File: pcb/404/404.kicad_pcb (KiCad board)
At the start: 2 copper layers, 52 x 63 mm, 43 parts, among them J1 Conn_01x04, Q1 BC846, U1 RC4558

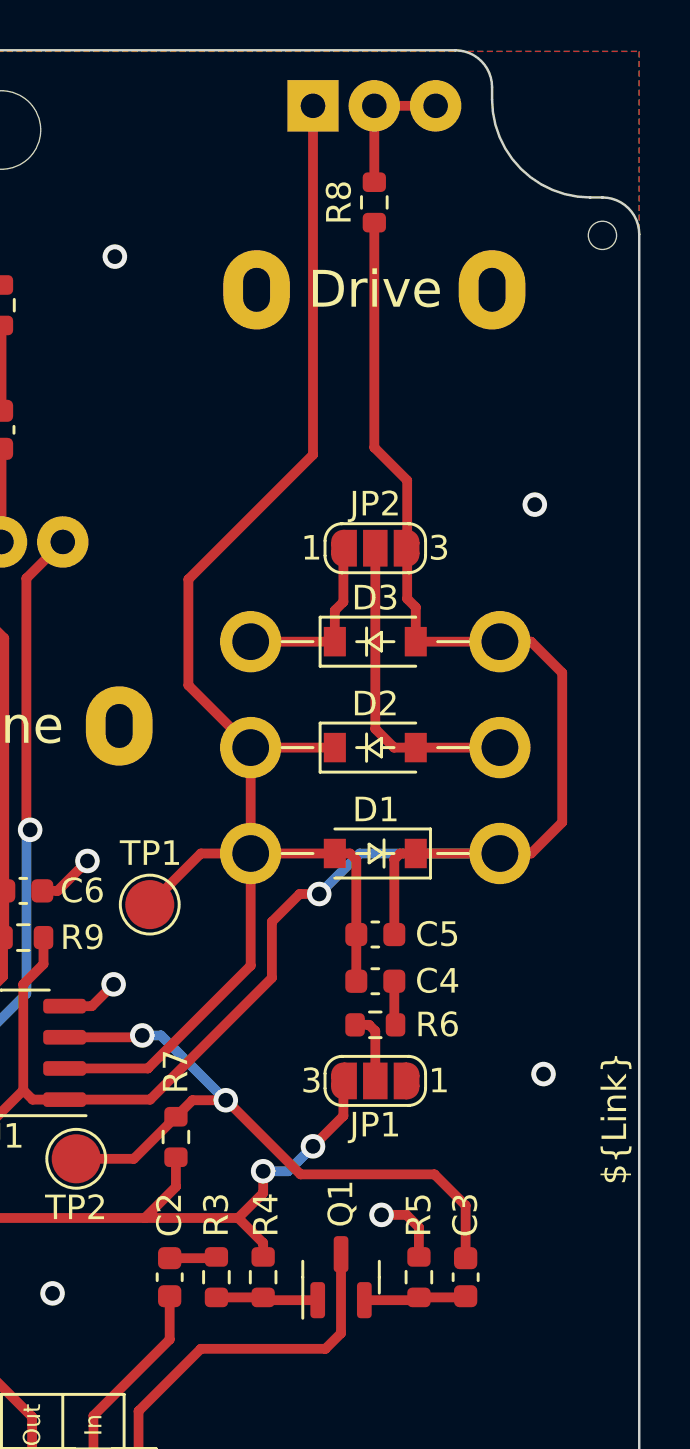
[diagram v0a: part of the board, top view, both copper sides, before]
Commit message: [404] Rename board; Update silk jumper description
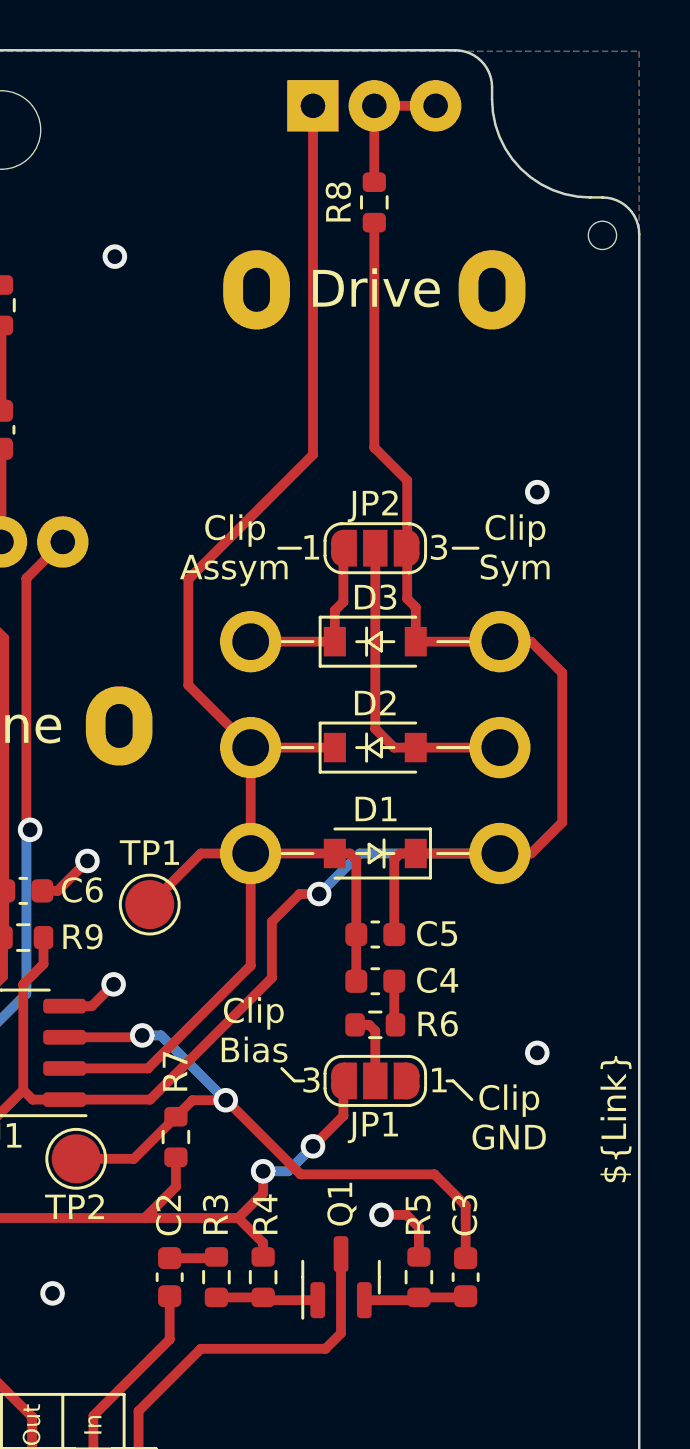
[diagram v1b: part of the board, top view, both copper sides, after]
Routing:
- net Net-(C4-Pad1): track 66.1 -> 65.3 mm
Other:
- board text added: "Clip Assym"
- board text added: "Clip Bias"
- board text added: "Clip GND"
- board text added: "Clip Sym"
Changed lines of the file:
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@@
   (gr_line (start 152 122.295) (end 152 124.561) (layer "F.SilkS") (width 0.12))
   (gr_line (start 144.5 122.295) (end 144.5 124.561) (layer "F.SilkS") (width 0.12))
+  (gr_line (start 167.915 87.799) (end 168.931 87.799) (layer "F.SilkS") (width 0.12))
+  (gr_line (start 161.692 87.799) (end 160.803 87.799) (layer "F.SilkS") (width 0.12))
   (gr_line (start 149.5 122.295) (end 149.5 124.561) (layer "F.SilkS") (width 0.12))
+  (gr_line (start 167.915 109.516) (end 168.677 110.278) (layer "F.SilkS") (width 0.12))
   (gr_line (start 144.5 122.295) (end 154.5 122.295) (layer "F.SilkS") (width 0.12))
   (gr_line (start 147 122.295) (end 147 124.545) (layer "F.SilkS") (width 0.12))
+  (gr_line (start 161.819 109.516) (end 161.438 109.516) (layer "F.SilkS") (width 0.12))
   (gr_line (start 154.5 122.295) (end 154.5 124.561) (layer "F.SilkS") (width 0.12))
+  (gr_line (start 161.438 109.516) (end 160.93 109.008) (layer "F.SilkS") (width 0.12))
+  (gr_line (start 167.661 109.516) (end 167.915 109.516) (layer "F.SilkS") (width 0.12))
   (gr_line (start 149.5 67.545) (end 149.5 130.545) (layer "Eco1.User") (width 0.15))
   (gr_line (start 125 73.5) (end 125.5 73.5) (layer "Edge.Cuts") (width 0.1))
@@
     (effects (font (size 1.5 1.5) (thickness 0.3)))
   )
+  (gr_text "Clip\nGND" (at 170.201 111.04) (layer "F.SilkS")
+    (effects (font (size 1 1) (thickness 0.15)))
+  )
+  (gr_text "Clip\nBias" (at 159.787 107.484) (layer "F.SilkS")
+    (effects (font (size 1 1) (thickness 0.15)))
+  )
   (gr_text "${Commit}" (at 163 127.545) (layer "F.SilkS")
     (effects (font (size 1 1) (thickness 0.2)))
@@
   (gr_text "Out" (at 150.75 123.545 90) (layer "F.SilkS")
     (effects (font (size 0.7 0.7) (thickness 0.13)))
+  )
+  (gr_text "Clip\nSym" (at 170.455 87.799) (layer "F.SilkS")
+    (effects (font (size 1 1) (thickness 0.15)))
   )
   (gr_text "Vol" (at 134.26 77.258) (layer "F.SilkS")
     (effects (font (size 1.5 1.5) (thickness 0.3)))
+  )
+  (gr_text "Clip\nAssym" (at 159.025 87.799) (layer "F.SilkS")
+    (effects (font (size 1 1) (thickness 0.15)))
   )
   (gr_text "Drive" (at 164.74 77.258) (layer "F.SilkS")
@@
   (via (at 153.0052 100.5498) (size 1) (drill 0.6) (layers "F.Cu" "B.Cu") (net 2))
   (via (at 154.1228 75.9118) (size 1) (drill 0.6) (layers "F.Cu" "B.Cu") (free) (net 2))
-  (via (at 171.598 109.2366) (size 1) (drill 0.6) (layers "F.Cu" "B.Cu") (free) (net 2))
+  (via (at 171.344 108.373) (size 1) (drill 0.6) (layers "F.Cu" "B.Cu") (free) (net 2))
   (via (at 127.656 101.8706) (size 1) (drill 0.6) (layers "F.Cu" "B.Cu") (free) (net 2))
   (via (at 154.072 105.579) (size 1) (drill 0.6) (layers "F.Cu" "B.Cu") (net 2))
   (via (at 151.5828 118.1774) (size 1) (drill 0.6) (layers "F.Cu" "B.Cu") (free) (net 2))
   (via (at 145 75.9118) (size 1) (drill 0.6) (layers "F.Cu" "B.Cu") (free) (net 2))
-  (via (at 171.2424 86.021) (size 1) (drill 0.6) (layers "F.Cu" "B.Cu") (free) (net 2))
+  (via (at 171.344 85.513) (size 1) (drill 0.6) (layers "F.Cu" "B.Cu") (free) (net 2))
   (via (at 164.994 114.977) (size 1) (drill 0.6) (layers "F.Cu" "B.Cu") (net 2))
   (segment (start 153.25 123.165) (end 153.25 126.975) (width 0.4) (layer "F.Cu") (net 3))
@@
   (segment (start 166.4055 118.4545) (end 166.518 118.342) (width 0.4) (layer "F.Cu") (net 6))
   (segment (start 166.518 118.342) (end 168.373 118.342) (width 0.4) (layer "F.Cu") (net 6))
-  (segment (start 166.568 118.292) (end 166.518 118.342) (width 0.4) (layer "F.Cu") (net 6))
   (segment (start 164.293 118.4545) (end 166.4055 118.4545) (width 0.4) (layer "F.Cu") (net 6))
   (segment (start 168.423 114.596) (end 168.423 116.742) (width 0.4) (layer "F.Cu") (net 7))
@@
   (segment (start 158.644 110.3034) (end 156.0024 107.6618) (width 0.4) (layer "B.Cu") (net 7))
   (segment (start 165.515 107.18) (end 165.565 107.23) (width 0.4) (layer "F.Cu") (net 8))
-  (segment (start 165.565 105.502) (end 165.515 105.452) (width 0.4) (layer "F.Cu") (net 8))
   (segment (start 165.515 105.452) (end 165.515 107.18) (width 0.4) (layer "F.Cu") (net 8))
   (segment (start 159.66 95.927) (end 163.09 95.927) (width 0.4) (layer "F.Cu") (net 9))
@@
   (segment (start 157.12 89.069) (end 157.12 93.387) (width 0.4) (layer "F.Cu") (net 9))
   (segment (start 155.5452 102.3278) (end 157.628 100.245) (width 0.4) (layer "F.Cu") (net 9))
-  (segment (start 158.898 95.927) (end 159.66 95.927) (width 0.4) (layer "F.Cu") (net 9))
   (segment (start 162.2 83.989) (end 157.12 89.069) (width 0.4) (layer "F.Cu") (net 9))
   (segment (start 157.12 93.387) (end 159.66 95.927) (width 0.4) (layer "F.Cu") (net 9))
@@
   (segment (start 164.7 72.877) (end 164.7 69.765) (width 0.4) (layer "F.Cu") (net 20))
   (segment (start 164.7 69.765) (end 167.2 69.765) (width 0.4) (layer "F.Cu") (net 20))
-  (segment (start 164.7 69.765) (end 164.651663 69.765) (width 0.4) (layer "F.Cu") (net 20))
   (segment (start 146.925 107.738) (end 143.467 107.738) (width 0.4) (layer "F.Cu") (net 21))
   (segment (start 148.865 107.611) (end 148.738 107.738) (width 0.4) (layer "F.Cu") (net 21))

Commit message: [404] Export gerbers/pos/bom
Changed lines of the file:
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@@
       (layerselection 0x00010fc_ffffffff)
       (disableapertmacros false)
-      (usegerberextensions false)
-      (usegerberattributes true)
-      (usegerberadvancedattributes true)
-      (creategerberjobfile true)
+      (usegerberextensions true)
+      (usegerberattributes false)
+      (usegerberadvancedattributes false)
+      (creategerberjobfile false)
       (svguseinch false)
       (svgprecision 6)
       (excludeedgelayer true)
       (plotframeref false)
-      (viasonmask false)
+      (viasonmask true)
       (mode 1)
       (useauxorigin false)
@@
       (plotinvisibletext false)
       (sketchpadsonfab false)
-      (subtractmaskfromsilk false)
+      (subtractmaskfromsilk true)
       (outputformat 1)
       (mirror false)
-      (drillshape 1)
+      (drillshape 0)
       (scaleselection 1)
-      (outputdirectory "")
-    )
-  )
-  (property "Commit" "Commit")
+      (outputdirectory "../../_gitignored/Gerbers/404/Pos/")
+    )
+  )
+  (property "Commit" "87d2bbb")
   (property "Link" "gitlab.com/Chrismettal/pedaldev")
   (property "Name" "404")
@@
     (fp_line (start -1.6 0.8) (end -1.6 -0.8) (layer "F.Fab") (width 0.1))
     (fp_line (start 1.6 0.8) (end -1.6 0.8) (layer "F.Fab") (width 0.1))
-    (pad "1" smd roundrect (at -1.475 0 270) (size 1.15 1.8) (layers "F.Cu" "F.Paste" "F.Mask") (roundrect_rratio 0.217391)
+    (pad "1" smd roundrect (at -1.475 0 270) (size 1.15 1.8) (layers "F.Cu" "F.Paste" "F.Mask") (roundrect_rratio 0.2173913043)
       (net 22 "+4V5") (pintype "passive"))
-    (pad "2" smd roundrect (at 1.475 0 270) (size 1.15 1.8) (layers "F.Cu" "F.Paste" "F.Mask") (roundrect_rratio 0.217391)
+    (pad "2" smd roundrect (at 1.475 0 270) (size 1.15 1.8) (layers "F.Cu" "F.Paste" "F.Mask") (roundrect_rratio 0.2173913043)
       (net 2 "GND") (pintype "passive"))
     (model "${KICAD6_3DMODEL_DIR}/Capacitor_SMD.3dshapes/C_1206_3216Metric.wrl"
@@
     (fp_line (start 0 -1.35) (end 0.625 -2.35) (layer "F.Fab") (width 0.1))
     (fp_line (start -2.45 3.4) (end 9.95 3.4) (layer "F.Fab") (width 0.1))
-    (pad "1" thru_hole roundrect (at 0 0) (size 1.7 1.95) (drill 0.95) (layers *.Cu *.Mask) (roundrect_rratio 0.147059)
+    (pad "1" thru_hole roundrect (at 0 0) (size 1.7 1.95) (drill 0.95) (layers *.Cu *.Mask) (roundrect_rratio 0.1470588235)
       (net 2 "GND") (pinfunction "Pin_1") (pintype "passive"))
     (pad "2" thru_hole oval (at 2.5 0) (size 1.7 1.95) (drill 0.95) (layers *.Cu *.Mask)

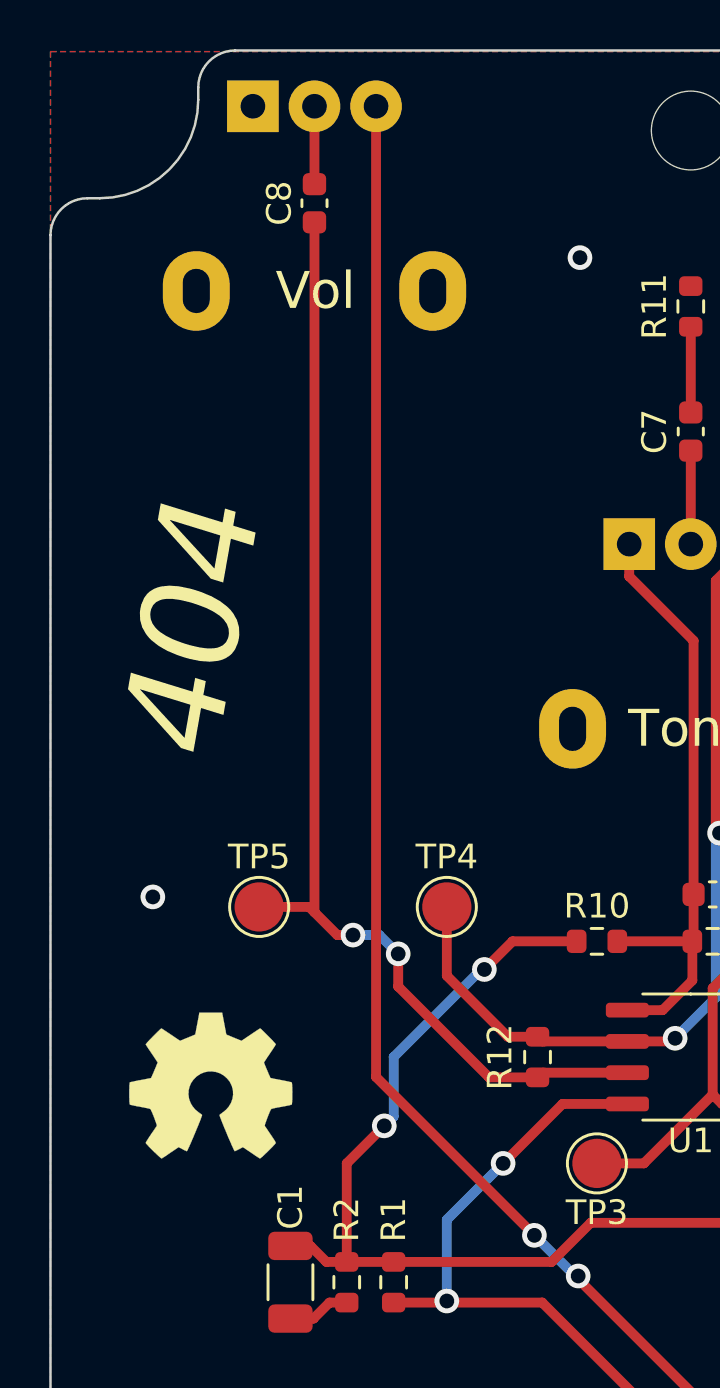
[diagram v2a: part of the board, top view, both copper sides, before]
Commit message: [All] Find out that the upper left pot is 0,08mm off on all designs
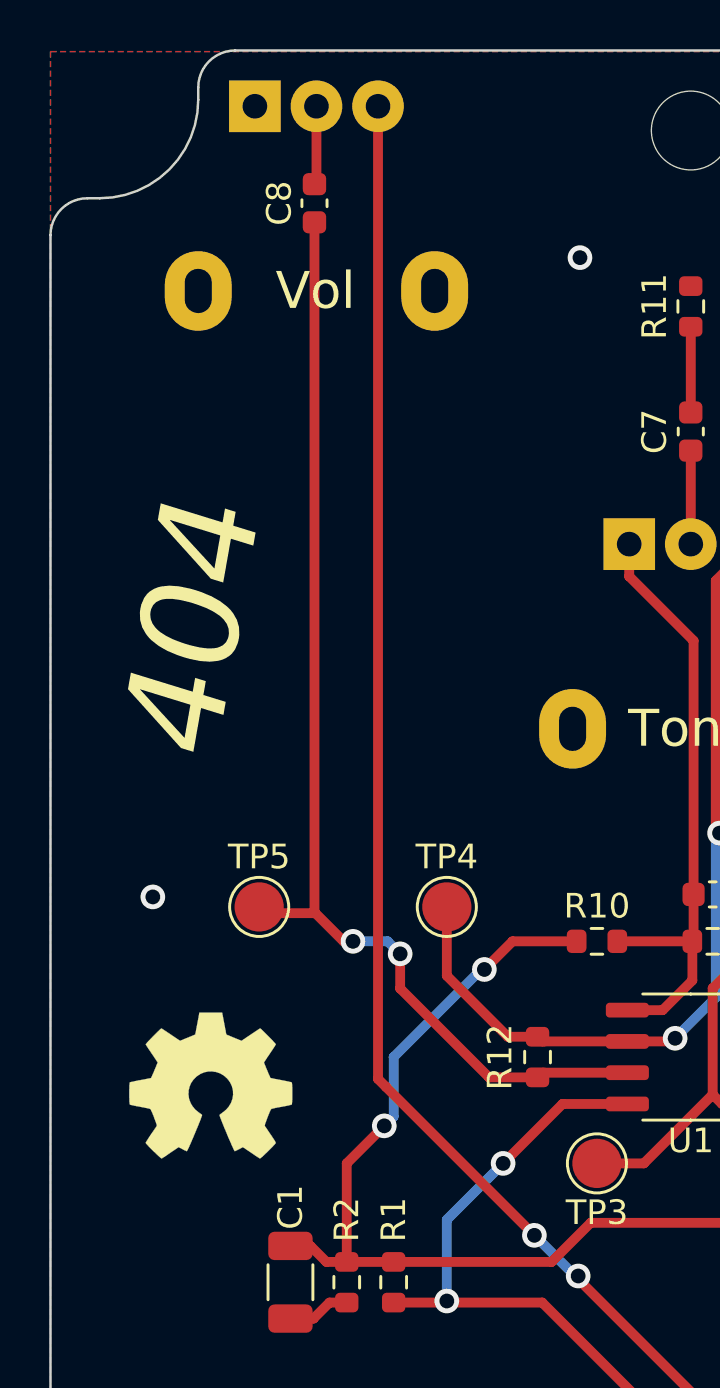
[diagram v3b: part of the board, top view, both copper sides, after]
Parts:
- moved RV3 0.08 mm to (131.8, 69.8)
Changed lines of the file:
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@@
       (drillshape 0)
       (scaleselection 1)
-      (outputdirectory "../../_gitignored/Gerbers/404/Pos/")
-    )
-  )
-  (property "Commit" "87d2bbb")
+      (outputdirectory "production_files/grb/")
+    )
+  )
+  (property "Commit" "")
   (property "Link" "gitlab.com/Chrismettal/pedaldev")
   (property "Name" "404")
@@
   )
   (footprint "MeineBib:Potentiometer_Alpha_RD901F-40-00D_Single_Vertical" (layer "B.Cu")
-    (at 131.72 69.765 -90)
+    (at 131.8 69.765 -90)
     (descr "Potentiometer, vertical, 9mm, single, http://www.taiwanalpha.com.tw/downloads?target=products&id=113")
     (tags "potentiometer vertical 9mm single")
@@
   (segment (start 156.358 118.292) (end 156.358 120.057) (width 0.4) (layer "F.Cu") (net 3))
   (segment (start 156.358 120.057) (end 153.25 123.165) (width 0.4) (layer "F.Cu") (net 3))
+  (segment (start 136.8 109.262) (end 137.1175 109.5795) (width 0.4) (layer "F.Cu") (net 4))
+  (segment (start 136.8 69.765) (end 136.8 109.262) (width 0.4) (layer "F.Cu") (net 4))
   (segment (start 150.75 123.212) (end 150.75 126.975) (width 0.4) (layer "F.Cu") (net 4))
-  (segment (start 136.72 69.765) (end 136.72 109.182) (width 0.4) (layer "F.Cu") (net 4))
-  (segment (start 136.72 109.182) (end 143.15 115.612) (width 0.4) (layer "F.Cu") (net 4))
+  (segment (start 137.1175 109.5795) (end 143.15 115.612) (width 0.4) (layer "F.Cu") (net 4))
   (segment (start 144.928 117.39) (end 150.75 123.212) (width 0.4) (layer "F.Cu") (net 4))
   (segment (start 144.928 117.263) (end 144.928 117.39) (width 0.4) (layer "F.Cu") (net 4))
@@
   (segment (start 164.105 100.245) (end 169.82 100.245) (width 0.4) (layer "B.Cu") (net 10))
   (segment (start 149.5 82.198) (end 149.5 78.718) (width 0.4) (layer "F.Cu") (net 11))
+  (segment (start 135.784 103.674) (end 135.403 103.674) (width 0.4) (layer "F.Cu") (net 12))
+  (segment (start 134.18 102.531) (end 134.22 102.491) (width 0.4) (layer "F.Cu") (net 12))
+  (segment (start 137.6995 104.182) (end 137.6995 105.5895) (width 0.4) (layer "F.Cu") (net 12))
+  (segment (start 131.974 102.277) (end 132.228 102.531) (width 0.4) (layer "F.Cu") (net 12))
+  (segment (start 146.925 109.008) (end 143.467 109.008) (width 0.4) (layer "F.Cu") (net 12))
+  (segment (start 135.403 103.674) (end 134.22 102.491) (width 0.4) (layer "F.Cu") (net 12))
+  (segment (start 137.6995 105.5895) (end 141.308 109.198) (width 0.4) (layer "F.Cu") (net 12))
+  (segment (start 134.22 74.477) (end 134.22 102.491) (width 0.4) (layer "F.Cu") (net 12))
   (segment (start 141.308 109.198) (end 143.277 109.198) (width 0.4) (layer "F.Cu") (net 12))
-  (segment (start 131.974 102.277) (end 134.006 102.277) (width 0.4) (layer "F.Cu") (net 12))
-  (segment (start 137.6195 104.182) (end 137.6195 105.5095) (width 0.4) (layer "F.Cu") (net 12))
-  (segment (start 134.22 102.491) (end 135.149 103.42) (width 0.4) (layer "F.Cu") (net 12))
-  (segment (start 146.925 109.008) (end 143.467 109.008) (width 0.4) (layer "F.Cu") (net 12))
-  (segment (start 137.6195 105.5095) (end 141.308 109.198) (width 0.4) (layer "F.Cu") (net 12))
-  (segment (start 134.22 74.477) (end 134.22 102.491) (width 0.4) (layer "F.Cu") (net 12))
-  (segment (start 135.149 103.42) (end 135.784 103.42) (width 0.4) (layer "F.Cu") (net 12))
   (segment (start 143.467 109.008) (end 143.277 109.198) (width 0.4) (layer "F.Cu") (net 12))
-  (segment (start 134.006 102.277) (end 134.22 102.491) (width 0.4) (layer "F.Cu") (net 12))
-  (via (at 137.6195 104.182) (size 1) (drill 0.6) (layers "F.Cu" "B.Cu") (net 12))
-  (via (at 135.784 103.42) (size 1) (drill 0.6) (layers "F.Cu" "B.Cu") (net 12))
-  (segment (start 136.8575 103.42) (end 137.6195 104.182) (width 0.4) (layer "B.Cu") (net 12))
-  (segment (start 135.784 103.42) (end 136.8575 103.42) (width 0.4) (layer "B.Cu") (net 12))
+  (segment (start 132.228 102.531) (end 134.18 102.531) (width 0.4) (layer "F.Cu") (net 12))
+  (via (at 137.6995 104.182) (size 1) (drill 0.6) (layers "F.Cu" "B.Cu") (net 12))
+  (via (at 135.784 103.674) (size 1) (drill 0.6) (layers "F.Cu" "B.Cu") (net 12))
+  (segment (start 137.1915 103.674) (end 135.784 103.674) (width 0.4) (layer "B.Cu") (net 12))
+  (segment (start 137.6995 104.182) (end 137.1915 103.674) (width 0.4) (layer "B.Cu") (net 12))
   (segment (start 146.925 106.468) (end 148.357 106.468) (width 0.4) (layer "F.Cu") (net 13))
   (segment (start 149.614 91.469) (end 147 88.855) (width 0.4) (layer "F.Cu") (net 13))
@@
   (segment (start 160.2805 118.4545) (end 160.168 118.342) (width 0.4) (layer "F.Cu") (net 15))
   (segment (start 149.5 83.748) (end 149.5 87.545) (width 0.4) (layer "F.Cu") (net 16))
-  (segment (start 134.22 72.927) (end 134.22 69.765) (width 0.4) (layer "F.Cu") (net 17))
+  (segment (start 134.3 69.765) (end 134.3 72.847) (width 0.4) (layer "F.Cu") (net 17))
+  (segment (start 134.3 72.847) (end 134.22 72.927) (width 0.4) (layer "F.Cu") (net 17))
   (segment (start 166.39 95.927) (end 169.82 95.927) (width 0.4) (layer "F.Cu") (net 18))
   (segment (start 164.74 95.165) (end 165.502 95.927) (width 0.4) (layer "F.Cu") (net 18))
